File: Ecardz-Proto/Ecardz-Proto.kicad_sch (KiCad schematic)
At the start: 0 parts

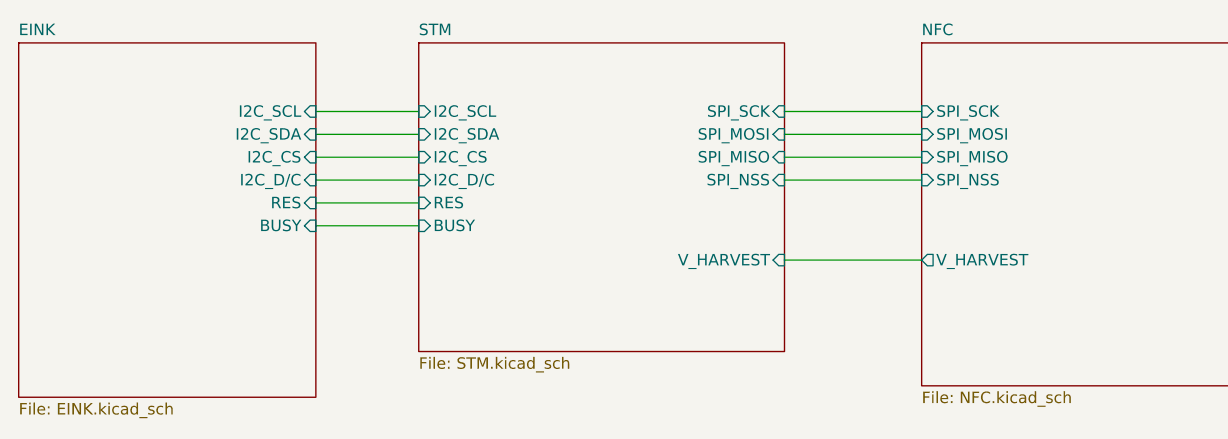
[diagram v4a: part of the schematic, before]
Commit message: added STM and rpi pin connections.
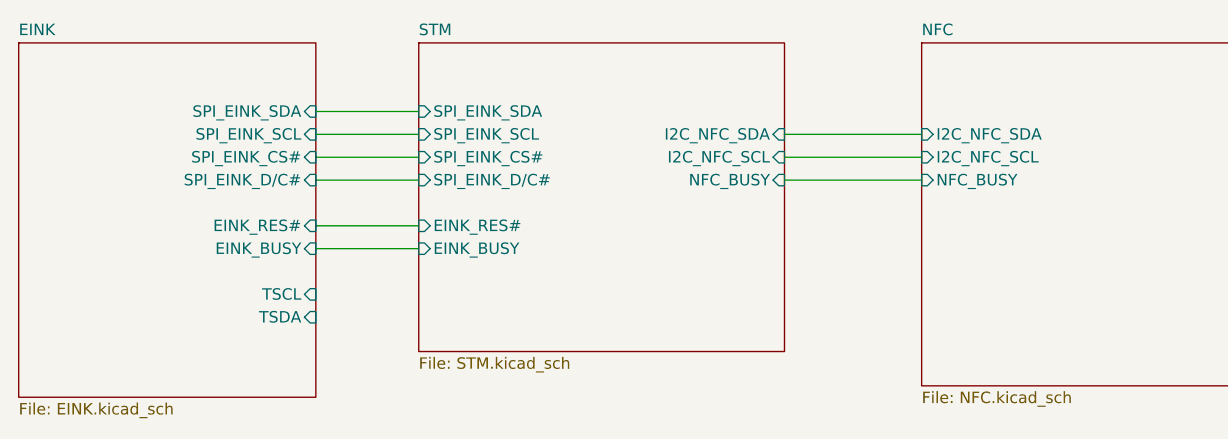
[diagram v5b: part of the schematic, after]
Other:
- sheet EINK ports: added EINK_BUSY, EINK_RES#, SPI_EINK_CS#, SPI_EINK_D/C#, SPI_EINK_SCL, SPI_EINK_SDA, TSCL, TSDA; removed BUSY, I2C_CS, I2C_D/C, I2C_SCL, I2C_SDA, RES
- sheet NFC ports: added I2C_NFC_SCL, I2C_NFC_SDA, NFC_BUSY; removed SPI_MISO, SPI_MOSI, SPI_NSS, SPI_SCK, V_HARVEST
- sheet STM ports: added EINK_BUSY, EINK_RES#, I2C_NFC_SCL, I2C_NFC_SDA, NFC_BUSY, SPI_EINK_CS#, SPI_EINK_D/C#, SPI_EINK_SCL, SPI_EINK_SDA; removed BUSY, I2C_CS, I2C_D/C, I2C_SCL, I2C_SDA, RES, SPI_MISO, SPI_MOSI, SPI_NSS, SPI_SCK, V_HARVEST
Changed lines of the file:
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@@
+	(wire
+		(pts
+			(xy 101.6 71.12) (xy 113.03 71.12)
+		)
+		(stroke
+			(width 0)
+			(type default)
+		)
+	)
+	(wire
+		(pts
+			(xy 101.6 78.74) (xy 113.03 78.74)
+		)
+		(stroke
+			(width 0)
+			(type default)
+		)
+	)
+	(wire
+		(pts
+			(xy 101.6 73.66) (xy 113.03 73.66)
+		)
+		(stroke
+			(width 0)
+			(type default)
+		)
+	)
+	(wire
+		(pts
+			(xy 153.67 78.74) (xy 168.91 78.74)
+		)
+		(stroke
+			(width 0)
+			(type default)
+		)
+	)
 	(wire
 		(pts
@@
 	(wire
 		(pts
-			(xy 153.67 87.63) (xy 168.91 87.63)
-		)
-		(stroke
-			(width 0)
-			(type default)
-		)
-	)
-	(wire
-		(pts
-			(xy 101.6 71.12) (xy 113.03 71.12)
+			(xy 101.6 86.36) (xy 113.03 86.36)
+		)
+		(stroke
+			(width 0)
+			(type default)
+		)
+	)
+	(wire
+		(pts
+			(xy 101.6 83.82) (xy 113.03 83.82)
+		)
+		(stroke
+			(width 0)
+			(type default)
+		)
+	)
+	(wire
+		(pts
+			(xy 153.67 73.66) (xy 168.91 73.66)
 		)
 		(stroke
@@
 		(pts
 			(xy 101.6 76.2) (xy 113.03 76.2)
-		)
-		(stroke
-			(width 0)
-			(type default)
-		)
-	)
-	(wire
-		(pts
-			(xy 101.6 83.82) (xy 113.03 83.82)
-		)
-		(stroke
-			(width 0)
-			(type default)
-		)
-	)
-	(wire
-		(pts
-			(xy 101.6 81.28) (xy 113.03 81.28)
-		)
-		(stroke
-			(width 0)
-			(type default)
-		)
-	)
-	(wire
-		(pts
-			(xy 153.67 73.66) (xy 168.91 73.66)
-		)
-		(stroke
-			(width 0)
-			(type default)
-		)
-	)
-	(wire
-		(pts
-			(xy 101.6 73.66) (xy 113.03 73.66)
-		)
-		(stroke
-			(width 0)
-			(type default)
-		)
-	)
-	(wire
-		(pts
-			(xy 153.67 78.74) (xy 168.91 78.74)
-		)
-		(stroke
-			(width 0)
-			(type default)
-		)
-	)
-	(wire
-		(pts
-			(xy 101.6 78.74) (xy 113.03 78.74)
-		)
-		(stroke
-			(width 0)
-			(type default)
-		)
-	)
-	(wire
-		(pts
-			(xy 153.67 71.12) (xy 168.91 71.12)
 		)
 		(stroke
@@
 			)
 		)
-		(pin "SPI_MISO" input
+		(pin "I2C_NFC_SDA" input
+			(at 168.91 73.66 180)
+			(effects
+				(font
+					(size 1.27 1.27)
+				)
+				(justify left)
+			)
+		)
+		(pin "NFC_BUSY" input
+			(at 168.91 78.74 180)
+			(effects
+				(font
+					(size 1.27 1.27)
+				)
+				(justify left)
+			)
+		)
+		(pin "I2C_NFC_SCL" input
 			(at 168.91 76.2 180)
-			(effects
-				(font
-					(size 1.27 1.27)
-				)
-				(justify left)
-			)
-		)
-		(pin "SPI_SCK" input
-			(at 168.91 71.12 180)
-			(effects
-				(font
-					(size 1.27 1.27)
-				)
-				(justify left)
-			)
-		)
-		(pin "SPI_MOSI" input
-			(at 168.91 73.66 180)
-			(effects
-				(font
-					(size 1.27 1.27)
-				)
-				(justify left)
-			)
-		)
-		(pin "SPI_NSS" input
-			(at 168.91 78.74 180)
-			(effects
-				(font
-					(size 1.27 1.27)
-				)
-				(justify left)
-			)
-		)
-		(pin "V_HARVEST" output
-			(at 168.91 87.63 180)
 			(effects
 				(font
@@
 			)
 		)
-		(pin "RES" input
-			(at 101.6 81.28 0)
-			(effects
-				(font
-					(size 1.27 1.27)
-				)
-				(justify right)
-			)
-		)
-		(pin "BUSY" input
+		(pin "EINK_RES#" input
 			(at 101.6 83.82 0)
 			(effects
@@
 			)
 		)
-		(pin "I2C_SCL" input
+		(pin "EINK_BUSY" input
+			(at 101.6 86.36 0)
+			(effects
+				(font
+					(size 1.27 1.27)
+				)
+				(justify right)
+			)
+		)
+		(pin "TSCL" input
+			(at 101.6 91.44 0)
+			(effects
+				(font
+					(size 1.27 1.27)
+				)
+				(justify right)
+			)
+		)
+		(pin "TSDA" input
+			(at 101.6 93.98 0)
+			(effects
+				(font
+					(size 1.27 1.27)
+				)
+				(justify right)
+			)
+		)
+		(pin "SPI_EINK_SDA" input
 			(at 101.6 71.12 0)
 			(effects
@@
 			)
 		)
-		(pin "I2C_CS" input
+		(pin "SPI_EINK_D{slash}C#" input
+			(at 101.6 78.74 0)
+			(effects
+				(font
+					(size 1.27 1.27)
+				)
+				(justify right)
+			)
+		)
+		(pin "SPI_EINK_SCL" input
+			(at 101.6 73.66 0)
+			(effects
+				(font
+					(size 1.27 1.27)
+				)
+				(justify right)
+			)
+		)
+		(pin "SPI_EINK_CS#" input
 			(at 101.6 76.2 0)
-			(effects
-				(font
-					(size 1.27 1.27)
-				)
-				(justify right)
-			)
-		)
-		(pin "I2C_D{slash}C" input
-			(at 101.6 78.74 0)
-			(effects
-				(font
-					(size 1.27 1.27)
-				)
-				(justify right)
-			)
-		)
-		(pin "I2C_SDA" input
-			(at 101.6 73.66 0)
 			(effects
 				(font
@@
 			)
 		)
-		(pin "I2C_SDA" input
+		(pin "SPI_EINK_SDA" input
+			(at 113.03 71.12 180)
+			(effects
+				(font
+					(size 1.27 1.27)
+				)
+				(justify left)
+			)
+		)
+		(pin "SPI_EINK_CS#" input
+			(at 113.03 76.2 180)
+			(effects
+				(font
+					(size 1.27 1.27)
+				)
+				(justify left)
+			)
+		)
+		(pin "SPI_EINK_SCL" input
 			(at 113.03 73.66 180)
 			(effects
@@
 			)
 		)
-		(pin "I2C_CS" input
-			(at 113.03 76.2 180)
-			(effects
-				(font
-					(size 1.27 1.27)
-				)
-				(justify left)
-			)
-		)
-		(pin "RES" input
-			(at 113.03 81.28 180)
-			(effects
-				(font
-					(size 1.27 1.27)
-				)
-				(justify left)
-			)
-		)
-		(pin "BUSY" input
+		(pin "SPI_EINK_D{slash}C#" input
+			(at 113.03 78.74 180)
+			(effects
+				(font
+					(size 1.27 1.27)
+				)
+				(justify left)
+			)
+		)
+		(pin "EINK_BUSY" input
+			(at 113.03 86.36 180)
+			(effects
+				(font
+					(size 1.27 1.27)
+				)
+				(justify left)
+			)
+		)
+		(pin "EINK_RES#" input
 			(at 113.03 83.82 180)
 			(effects
@@
 			)
 		)
-		(pin "I2C_SCL" input
-			(at 113.03 71.12 180)
-			(effects
-				(font
-					(size 1.27 1.27)
-				)
-				(justify left)
-			)
-		)
-		(pin "I2C_D{slash}C" input
-			(at 113.03 78.74 180)
-			(effects
-				(font
-					(size 1.27 1.27)
-				)
-				(justify left)
-			)
-		)
-		(pin "SPI_SCK" input
-			(at 153.67 71.12 0)
-			(effects
-				(font
-					(size 1.27 1.27)
-				)
-				(justify right)
-			)
-		)
-		(pin "SPI_MOSI" input
+		(pin "NFC_BUSY" input
+			(at 153.67 78.74 0)
+			(effects
+				(font
+					(size 1.27 1.27)
+				)
+				(justify right)
+			)
+		)
+		(pin "I2C_NFC_SCL" input
+			(at 153.67 76.2 0)
+			(effects
+				(font
+					(size 1.27 1.27)
+				)
+				(justify right)
+			)
+		)
+		(pin "I2C_NFC_SDA" input
 			(at 153.67 73.66 0)
 			(effects
 				(font
-					(size 1.27 1.27)
-				)
-				(justify right)
-			)
-		)
-		(pin "SPI_MISO" input
-			(at 153.67 76.2 0)
-			(effects
-				(font
-					(size 1.27 1.27)
-				)
-				(justify right)
-			)
-		)
-		(pin "SPI_NSS" input
-			(at 153.67 78.74 0)
-			(effects
-				(font
-					(size 1.27 1.27)
-				)
-				(justify right)
-			)
-		)
-		(pin "V_HARVEST" input
-			(at 153.67 87.63 0)
-			(effects
-				(font

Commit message: updated most footprints
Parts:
- added H1, H2, H3, H4: MountingHole_Pad, MountingHole:MountingHole_2.5mm_Pad_TopBottom, symbol Mechanical:MountingHole_Pad
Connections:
- new net GND: H1.1, H2.1, H3.1, H4.1

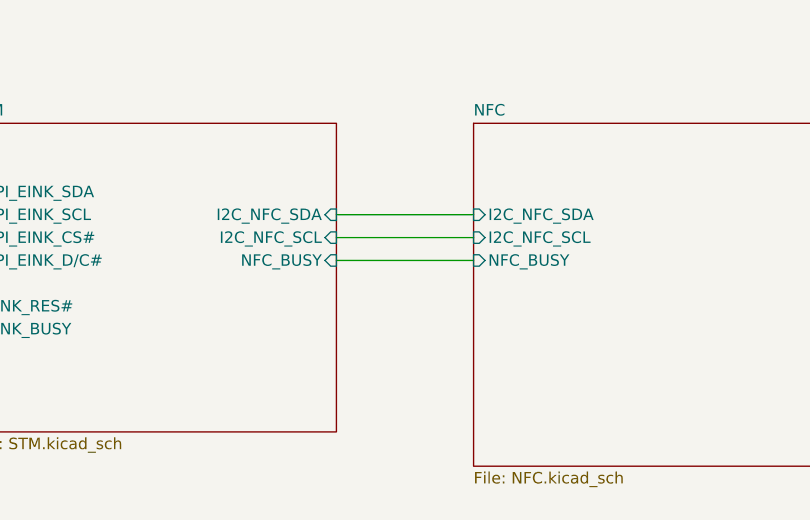
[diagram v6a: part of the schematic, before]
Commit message: added zener and extra cap footprints
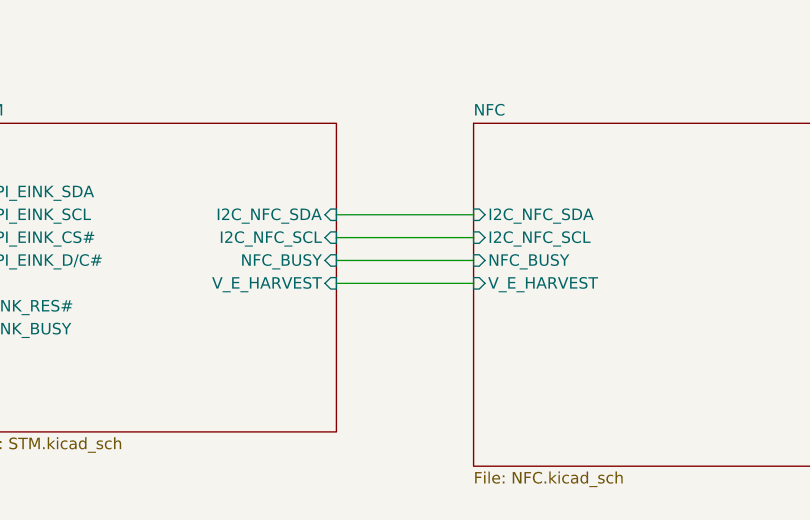
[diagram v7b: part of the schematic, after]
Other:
- sheet NFC ports: added V_E_HARVEST; removed none
- sheet STM ports: added V_E_HARVEST; removed none
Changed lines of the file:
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@@
+	(wire
+		(pts
+			(xy 153.67 81.28) (xy 168.91 81.28)
+		)
+		(stroke
+			(width 0)
+			(type default)
+		)
+	)
 	(wire
 		(pts
@@
 			)
 		)
+		(pin "V_E_HARVEST" input
+			(at 168.91 81.28 180)
+			(effects
+				(font
+					(size 1.27 1.27)
+				)
+				(justify left)
+			)
+		)
 		(instances
 			(project "Ecardz-Proto"
@@
 			(effects
 				(font
+					(size 1.27 1.27)
+				)
+				(justify right)
+			)
+		)
+		(pin "V_E_HARVEST" input
+			(at 153.67 81.28 0)
+			(effects
+				(font
